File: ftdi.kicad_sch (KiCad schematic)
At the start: 42 parts, among them U5 93LC56BT-I/OT, U6 FT2232HL, Y1 7M-12.000MAAJ

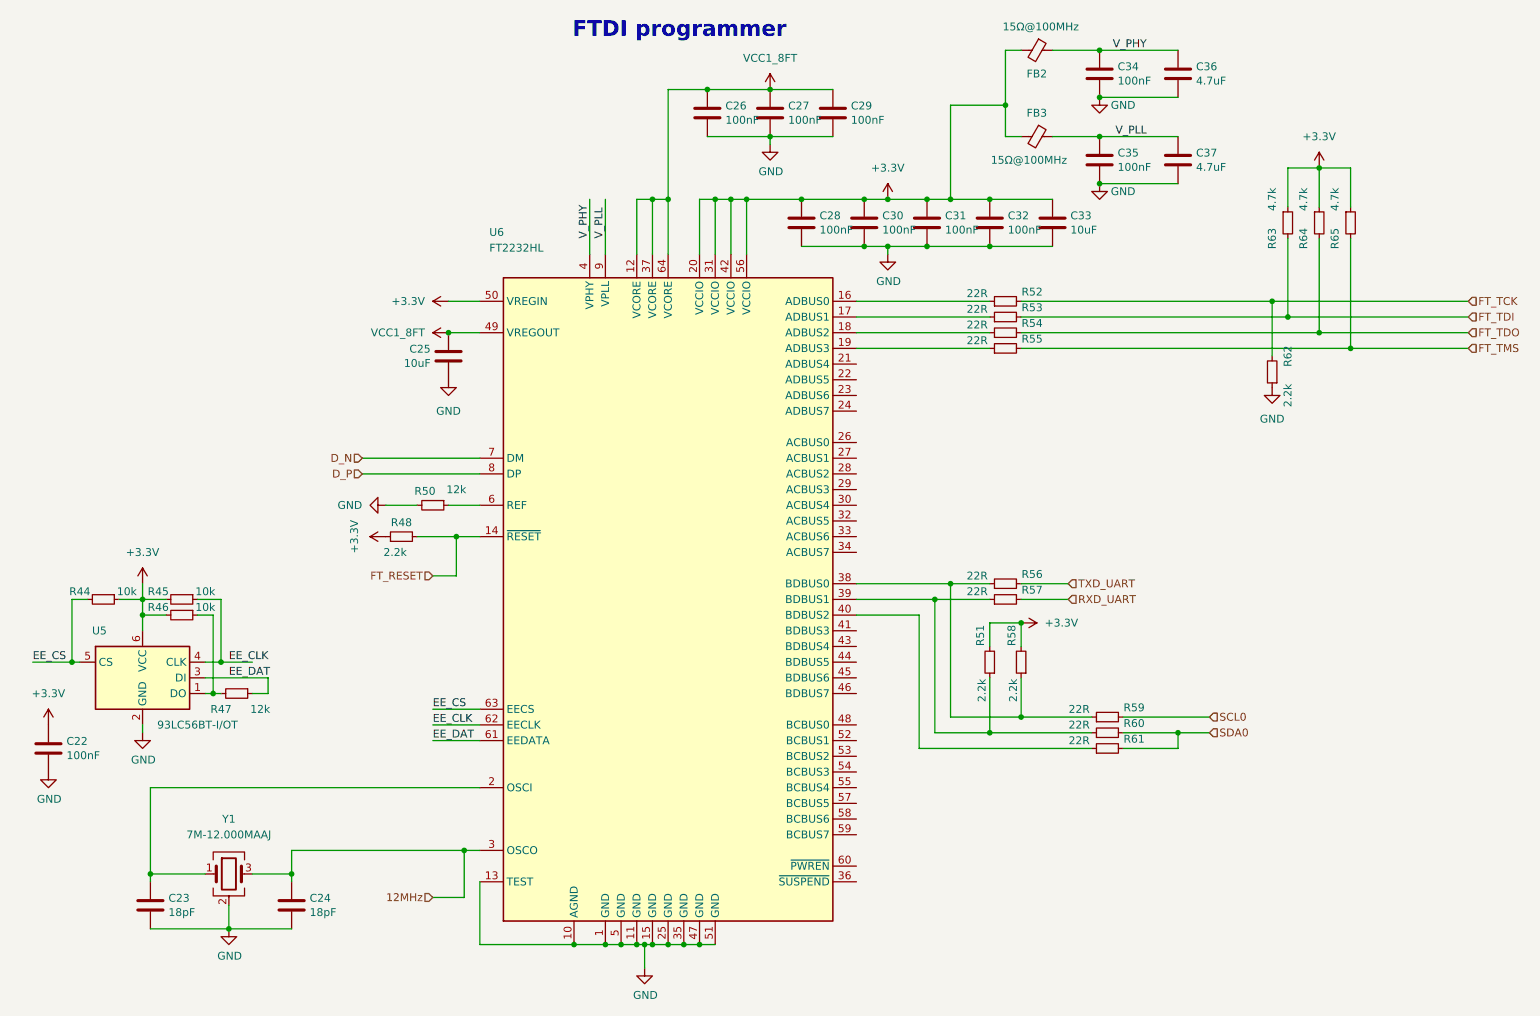
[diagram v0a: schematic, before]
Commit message: Fix dcr for schematics
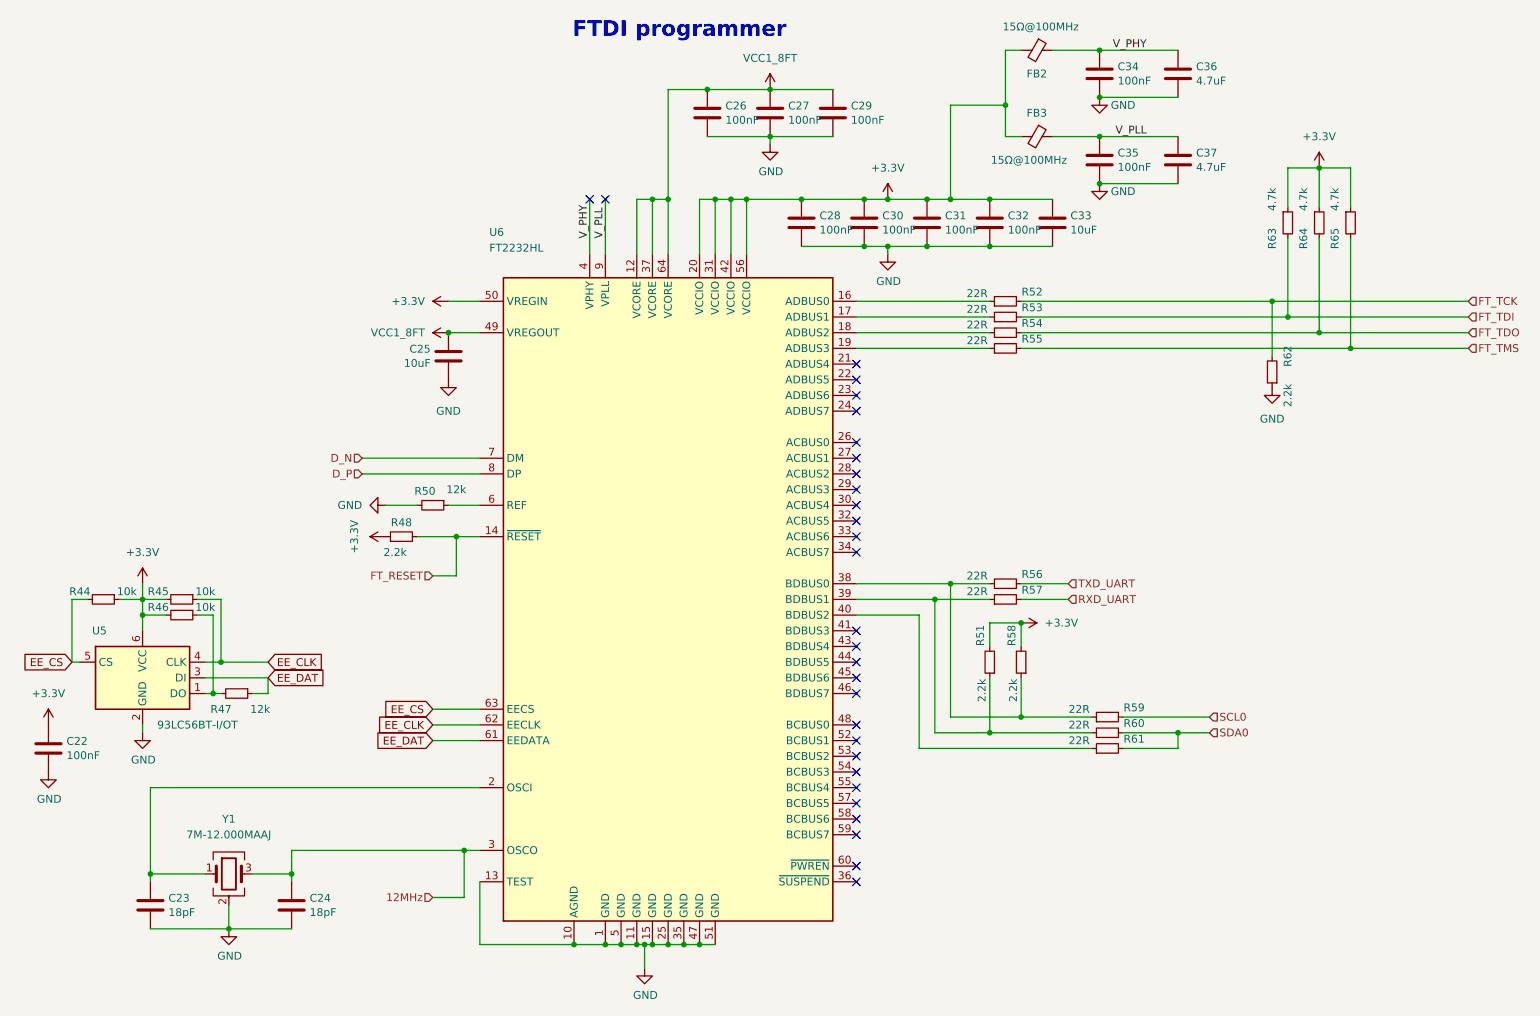
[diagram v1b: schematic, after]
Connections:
- no-connect marks 0 -> 29
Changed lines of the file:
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@@
-	)
-	(junction
-		(at 25.4 133.35)
-		(diameter 0)
-		(color 0 0 0 0)
 	)
 	(junction
@@
 	)
 	(junction
+		(at 49.53 133.35)
+		(diameter 0)
+		(color 0 0 0 0)
+	)
+	(junction
 		(at 36.83 125.73)
 		(diameter 0)
@@
 	)
 	(junction
-		(at 49.53 133.35)
-		(diameter 0)
-		(color 0 0 0 0)
-	)
-	(junction
 		(at 167.64 58.42)
 		(diameter 0)
@@
 		(color 0 0 0 0)
 	)
+	(no_connect
+		(at 152.4 97.79)
+	)
+	(no_connect
+		(at 152.4 102.87)
+	)
+	(no_connect
+		(at 152.4 128.27)
+	)
+	(no_connect
+		(at 152.4 158.75)
+	)
+	(no_connect
+		(at 152.4 146.05)
+	)
+	(no_connect
+		(at 152.4 105.41)
+	)
+	(no_connect
+		(at 152.4 138.43)
+	)
+	(no_connect
+		(at 152.4 110.49)
+	)
+	(no_connect
+		(at 152.4 156.21)
+	)
+	(no_connect
+		(at 152.4 143.51)
+	)
+	(no_connect
+		(at 152.4 113.03)
+	)
+	(no_connect
+		(at 152.4 161.29)
+	)
+	(no_connect
+		(at 152.4 166.37)
+	)
+	(no_connect
+		(at 152.4 92.71)
+	)
+	(no_connect
+		(at 152.4 148.59)
+	)
+	(no_connect
+		(at 152.4 107.95)
+	)
+	(no_connect
+		(at 152.4 87.63)
+	)
+	(no_connect
+		(at 152.4 115.57)
+	)
+	(no_connect
+		(at 152.4 90.17)
+	)
+	(no_connect
+		(at 152.4 133.35)
+	)
+	(no_connect
+		(at 111.76 58.42)
+	)
+	(no_connect
+		(at 152.4 130.81)
+	)
+	(no_connect
+		(at 152.4 168.91)
+	)
+	(no_connect
+		(at 152.4 151.13)
+	)
+	(no_connect
+		(at 152.4 85.09)
+	)
+	(no_connect
+		(at 152.4 100.33)
+	)
+	(no_connect
+		(at 152.4 153.67)
+	)
+	(no_connect
+		(at 152.4 135.89)
+	)
+	(no_connect
+		(at 109.22 58.42)
+	)
 	(wire
 		(pts
@@
 	(wire
 		(pts
-			(xy 25.4 133.35) (xy 19.05 133.35)
-		)
-		(stroke
-			(width 0)
-			(type default)
-		)
-	)
-	(wire
-		(pts
 			(xy 128.27 40.64) (xy 121.92 40.64)
 		)
@@
 	(wire
 		(pts
-			(xy 49.53 133.35) (xy 54.61 133.35)
-		)
-		(stroke
-			(width 0)
-			(type default)
-		)
-	)
-	(wire
-		(pts
 			(xy 129.54 58.42) (xy 132.08 58.42)
 		)
@@
 		(pts
 			(xy 54.61 138.43) (xy 57.15 138.43)
+		)
+		(stroke
+			(width 0)
+			(type default)
+		)
+	)
+	(wire
+		(pts
+			(xy 49.53 133.35) (xy 57.15 133.35)
 		)
 		(stroke
@@
 		)
 	)
-	(label "EE_DAT"
-		(at 83.82 146.05 0)
-		(effects
-			(font
-				(size 1.27 1.27)
-			)
-			(justify left bottom)
-		)
-	)
-	(label "EE_CLK"
-		(at 50.8 133.35 0)
-		(effects
-			(font
-				(size 1.27 1.27)
-			)
-			(justify left bottom)
-		)
-	)
-	(label "EE_CS"
-		(at 83.82 140.97 0)
-		(effects
-			(font
-				(size 1.27 1.27)
-			)
-			(justify left bottom)
-		)
-	)
 	(label "V_PHY"
 		(at 109.22 64.77 90)
@@
 		)
 	)
-	(label "EE_DAT"
-		(at 50.8 135.89 0)
-		(effects
-			(font
-				(size 1.27 1.27)
-			)
-			(justify left bottom)
-		)
-	)
-	(label "EE_CLK"
-		(at 83.82 143.51 0)
-		(effects
-			(font
-				(size 1.27 1.27)
-			)
-			(justify left bottom)
-		)
-	)
 	(label "V_PLL"
 		(at 111.76 64.77 90)
@@
 		)
 	)
-	(label "EE_CS"
-		(at 19.05 133.35 0)
-		(effects
-			(font
-				(size 1.27 1.27)
-			)
-			(justify left bottom)
-		)
-	)
 	(label "V_PHY"
 		(at 199.39 34.29 180)
@@
 		)
 	)
+	(global_label "EE_DAT"
+		(shape input)
+		(at 57.15 135.89 0)
+		(fields_autoplaced yes)
+		(effects
+			(font
+				(size 1.27 1.27)
+			)
+			(justify left)
+		)
+		(property "Intersheetrefs" "${INTERSHEET_REFS}"
+			(at 66.727 135.89 0)
+			(effects
+				(font
+					(size 1.27 1.27)
+				)
+				(justify left)
+				(hide yes)
+			)
+		)
+	)
+	(global_label "EE_CS"
+		(shape input)
+		(at 83.82 140.97 180)
+		(fields_autoplaced yes)
+		(effects
+			(font
+				(size 1.27 1.27)
+			)
+			(justify right)
+		)
+		(property "Intersheetrefs" "${INTERSHEET_REFS}"
+			(at 75.0897 140.97 0)
+			(effects
+				(font
+					(size 1.27 1.27)
+				)
+				(justify right)
+				(hide yes)
+			)
+		)
+	)
+	(global_label "EE_DAT"
+		(shape input)
+		(at 83.82 146.05 180)
+		(fields_autoplaced yes)
+		(effects
+			(font
+				(size 1.27 1.27)
+			)
+			(justify right)
+		)
+		(property "Intersheetrefs" "${INTERSHEET_REFS}"
+			(at 74.243 146.05 0)
+			(effects
+				(font
+					(size 1.27 1.27)
+				)
+				(justify right)
+				(hide yes)
+			)
+		)
+	)
+	(global_label "EE_CLK"
+		(shape input)
+		(at 83.82 143.51 180)
+		(fields_autoplaced yes)
+		(effects
+			(font
+				(size 1.27 1.27)
+			)
+			(justify right)
+		)
+		(property "Intersheetrefs" "${INTERSHEET_REFS}"
+			(at 74.0011 143.51 0)
+			(effects
+				(font
+					(size 1.27 1.27)
+				)
+				(justify right)
+				(hide yes)
+			)
+		)
+	)
+	(global_label "EE_CS"
+		(shape input)
+		(at 25.4 133.35 180)
+		(fields_autoplaced yes)
+		(effects
+			(font
+				(size 1.27 1.27)
+			)
+			(justify right)
+		)
+		(property "Intersheetrefs" "${INTERSHEET_REFS}"
+			(at 16.6697 133.35 0)
+			(effects
+				(font
+					(size 1.27 1.27)
+				)
+				(justify right)
+				(hide yes)
+			)
+		)
+	)
+	(global_label "EE_CLK"
+		(shape input)
+		(at 57.15 133.35 0)
+		(fields_autoplaced yes)
+		(effects
+			(font
+				(size 1.27 1.27)
+			)
+			(justify left)
+		)
+		(property "Intersheetrefs" "${INTERSHEET_REFS}"
+			(at 66.9689 133.35 0)
+			(effects
+				(font
+					(size 1.27 1.27)
+				)
+				(justify left)
+				(hide yes)
+			)
+		)
+	)
